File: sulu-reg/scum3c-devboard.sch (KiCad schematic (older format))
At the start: 36 parts, among them J1 Conn_02x11_Odd_Even, J2 Conn_02x10_Odd_Even, J3 Conn_02x05_Odd_Even, J4 73391-0060, U2 S-85S1AB18-I6T1U, U3 S-85S1AB11-I6T1U, U9AB1 ICM-20948

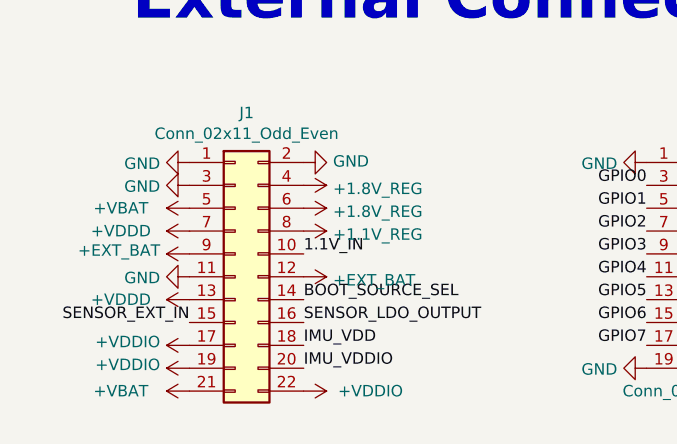
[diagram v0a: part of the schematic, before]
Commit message: Revert "rearranged some architecture"
This reverts commit c12dfdee068bb4749b85b6faf8935c1bd7e1da4a.
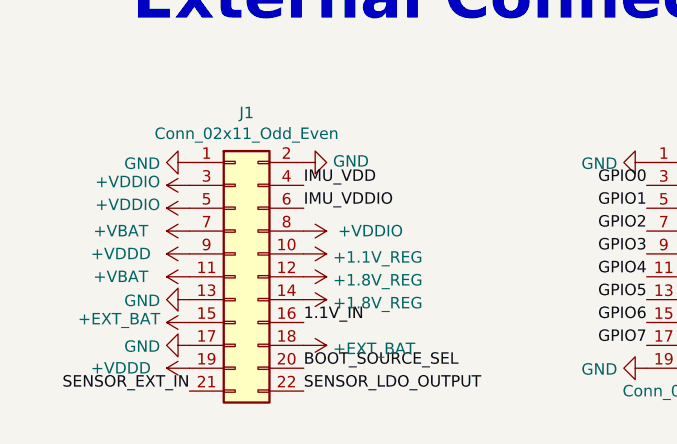
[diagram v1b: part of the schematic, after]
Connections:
- net +1.1V_REG: now also J1.10 (Pin_10); no longer J1.8 (Pin_8)
- net +1.8V_REG: now also J1.12 (Pin_12), J1.14 (Pin_14); no longer J1.4 (Pin_4), J1.6 (Pin_6)
- net +EXT_BAT: now also J1.15 (Pin_15), J1.18 (Pin_18); no longer J1.12 (Pin_12), J1.9 (Pin_9)
- net +VBAT: now also J1.11 (Pin_11), J1.7 (Pin_7); no longer J1.21 (Pin_21), J1.5 (Pin_5)
- net +VDDD: now also J1.19 (Pin_19), J1.9 (Pin_9); no longer J1.13 (Pin_13), J1.7 (Pin_7)
- net +VDDIO: now also J1.3 (Pin_3), J1.5 (Pin_5), J1.8 (Pin_8); no longer J1.17 (Pin_17), J1.19 (Pin_19), J1.22 (Pin_22)
- net 1.1V_IN: now also J1.16 (Pin_16); no longer J1.10 (Pin_10)
- net BOOT_SOURCE_SEL: now also J1.20 (Pin_20); no longer J1.14 (Pin_14)
- net GND: now also J1.13 (Pin_13), J1.17 (Pin_17); no longer J1.11 (Pin_11), J1.3 (Pin_3)
- net IMU_VDD: now also J1.4 (Pin_4); no longer J1.18 (Pin_18)
- net IMU_VDDIO: now also J1.6 (Pin_6); no longer J1.20 (Pin_20)
- net SENSOR_EXT_IN: now also J1.21 (Pin_21); no longer J1.15 (Pin_15)
- net SENSOR_LDO_OUTPUT: now also J1.22 (Pin_22); no longer J1.16 (Pin_16)
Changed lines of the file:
@@
 Text Label 1700 1750 2    50   ~ 0
 IMU_VDDIO
-Text Label 1800 7700 0    50   ~ 0
+Text Label 1800 7000 0    50   ~ 0
 IMU_VDDIO
 Text Label 3800 7300 0    50   ~ 0
@@
 Text Label 3800 7600 0    50   ~ 0
 GPIO15
-Text Label 1800 7600 0    50   ~ 0
+Text Label 1800 6900 0    50   ~ 0
 IMU_VDD
 NoConn ~ 1300 2950
@@
 	0    1    1    0
 $EndComp
-Text Label 1800 7400 0    50   ~ 0
+Text Label 1800 7700 0    50   ~ 0
 BOOT_SOURCE_SEL
 Text Label 5450 7150 0    50   ~ 0
@@
 	0    1    1    0
 $EndComp
-Text Label 1800 7500 0    50   ~ 0
+Text Label 1300 7800 2    50   ~ 0
+SENSOR_EXT_IN
+Text Label 1800 7800 0    50   ~ 0
 SENSOR_LDO_OUTPUT
 Text Label 4950 6950 2    50   ~ 0
@@
 RsTx
 $Comp
+L draft1library:+VDDIO #PWR?
+U 1 1 6076CC41
+P 1300 7000
+AR Path="/5F3B1D81/6076CC41" Ref="#PWR?"  Part="1"
+AR Path="/6076CC41" Ref="#PWR05"  Part="1"
+F 0 "#PWR05" H 1300 6850 50  0001 C CNN
+F 1 "+VDDIO" V 1315 7128 50  0000 L CNN
+F 2 "" H 1300 7000 50  0001 C CNN
+F 3 "" H 1300 7000 50  0001 C CNN
+	1    1300 7000
+	0    -1   -1   0
+$EndComp
+$Comp
+L draft1library:+VDDIO #PWR?
+U 1 1 6076D2AC
+P 1300 6900
+AR Path="/5F3B1D81/6076D2AC" Ref="#PWR?"  Part="1"
+AR Path="/6076D2AC" Ref="#PWR04"  Part="1"
+F 0 "#PWR04" H 1300 6750 50  0001 C CNN
+F 1 "+VDDIO" V 1315 7028 50  0000 L CNN
+F 2 "" H 1300 6900 50  0001 C CNN
+F 3 "" H 1300 6900 50  0001 C CNN
+	1    1300 6900
+	0    -1   -1   0
+$EndComp
+$Comp
 L draft1library:+VBAT #PWR?
 U 1 1 6076D7B9
-P 1300 7800
+P 1300 7100
 AR Path="/5F3B1D81/6076D7B9" Ref="#PWR?"  Part="1"
 AR Path="/5F41418C/6076D7B9" Ref="#PWR?"  Part="1"
 AR Path="/5F414989/6076D7B9" Ref="#PWR?"  Part="1"
 AR Path="/6076D7B9" Ref="#PWR06"  Part="1"
-F 0 "#PWR06" H 1300 7650 50  0001 C CNN
-F 1 "+VBAT" V 1300 8100 50  0000 C CNN
-F 2 "" H 1300 7800 50  0001 C CNN
-F 3 "" H 1300 7800 50  0001 C CNN
-	1    1300 7800
+F 0 "#PWR06" H 1300 6950 50  0001 C CNN
+F 1 "+VBAT" V 1300 7400 50  0000 C CNN
+F 2 "" H 1300 7100 50  0001 C CNN
+F 3 "" H 1300 7100 50  0001 C CNN
+	1    1300 7100
 	0    -1   -1   0
 $EndComp
@@
 L draft1library:+VBAT #PWR?
 U 1 1 6127ADAC
-P 1300 7000
+P 1300 7300
 AR Path="/5F3B1D81/6127ADAC" Ref="#PWR?"  Part="1"
 AR Path="/5F41418C/6127ADAC" Ref="#PWR?"  Part="1"
 AR Path="/5F414989/6127ADAC" Ref="#PWR?"  Part="1"
 AR Path="/6127ADAC" Ref="#PWR0107"  Part="1"
-F 0 "#PWR0107" H 1300 6850 50  0001 C CNN
-F 1 "+VBAT" V 1300 7300 50  0000 C CNN
-F 2 "" H 1300 7000 50  0001 C CNN
-F 3 "" H 1300 7000 50  0001 C CNN
-	1    1300 7000
+F 0 "#PWR0107" H 1300 7150 50  0001 C CNN
+F 1 "+VBAT" V 1300 7600 50  0000 C CNN
+F 2 "" H 1300 7300 50  0001 C CNN
+F 3 "" H 1300 7300 50  0001 C CNN
+	1    1300 7300
 	0    -1   -1   0
 $EndComp
@@
 L power:GND #PWR0108
 U 1 1 6127B18B
-P 1300 6900
-F 0 "#PWR0108" H 1300 6650 50  0001 C CNN
-F 1 "GND" V 1305 6772 50  0000 R CNN
-F 2 "" H 1300 6900 50  0001 C CNN
-F 3 "" H 1300 6900 50  0001 C CNN
-	1    1300 6900
+P 1300 7400
+F 0 "#PWR0108" H 1300 7150 50  0001 C CNN
+F 1 "GND" V 1305 7272 50  0000 R CNN
+F 2 "" H 1300 7400 50  0001 C CNN
+F 3 "" H 1300 7400 50  0001 C CNN
+	1    1300 7400
+	0    1    1    0
+$EndComp
+$Comp
+L power:GND #PWR0109
+U 1 1 6127B4FF
+P 1300 7600
+F 0 "#PWR0109" H 1300 7350 50  0001 C CNN
+F 1 "GND" V 1305 7472 50  0000 R CNN
+F 2 "" H 1300 7600 50  0001 C CNN
+F 3 "" H 1300 7600 50  0001 C CNN
+	1    1300 7600
 	0    1    1    0
 $EndComp
@@
 L draft1library:+1.1V_REG #PWR0110
 U 1 1 61280E78
-P 1800 7100
-F 0 "#PWR0110" H 1800 6950 50  0001 C CNN
-F 1 "+1.1V_REG" V 1815 7228 50  0000 L CNN
-F 2 "" H 1800 7100 50  0001 C CNN
-F 3 "" H 1800 7100 50  0001 C CNN
-	1    1800 7100
+P 1800 7200
+F 0 "#PWR0110" H 1800 7050 50  0001 C CNN
+F 1 "+1.1V_REG" V 1815 7328 50  0000 L CNN
+F 2 "" H 1800 7200 50  0001 C CNN
+F 3 "" H 1800 7200 50  0001 C CNN
+	1    1800 7200
 	0    1    1    0
 $EndComp
@@
 L draft1library:+1.8V_REG #PWR0111
 U 1 1 61281B91
-P 1800 6900
-F 0 "#PWR0111" H 1800 6750 50  0001 C CNN
-F 1 "+1.8V_REG" V 1815 7028 50  0000 L CNN
-F 2 "" H 1800 6900 50  0001 C CNN
-F 3 "" H 1800 6900 50  0001 C CNN
-	1    1800 6900
-	0    1    1    0
-$EndComp
-$Comp
-L draft1library:+1.8V_REG #PWR0112
-U 1 1 612829BE
-P 1800 7000
-F 0 "#PWR0112" H 1800 6850 50  0001 C CNN
-F 1 "+1.8V_REG" V 1815 7128 50  0000 L CNN
-F 2 "" H 1800 7000 50  0001 C CNN
-F 3 "" H 1800 7000 50  0001 C CNN
-	1    1800 7000
-	0    1    1    0
-$EndComp
-$Comp
-L draft1library:+EXT_BAT #PWR0113
-U 1 1 612835E6
 P 1800 7300
-F 0 "#PWR0113" H 1800 7150 50  0001 C CNN
-F 1 "+EXT_BAT" V 1815 7428 50  0000 L CNN
+F 0 "#PWR0111" H 1800 7150 50  0001 C CNN
+F 1 "+1.8V_REG" V 1815 7428 50  0000 L CNN
 F 2 "" H 1800 7300 50  0001 C CNN
 F 3 "" H 1800 7300 50  0001 C CNN
 	1    1800 7300
+	0    1    1    0
+$EndComp
+$Comp
+L draft1library:+1.8V_REG #PWR0112
+U 1 1 612829BE
+P 1800 7400
+F 0 "#PWR0112" H 1800 7250 50  0001 C CNN
+F 1 "+1.8V_REG" V 1815 7528 50  0000 L CNN
+F 2 "" H 1800 7400 50  0001 C CNN
+F 3 "" H 1800 7400 50  0001 C CNN
+	1    1800 7400
+	0    1    1    0
+$EndComp
+$Comp
+L draft1library:+EXT_BAT #PWR0113
+U 1 1 612835E6
+P 1800 7600
+F 0 "#PWR0113" H 1800 7450 50  0001 C CNN
+F 1 "+EXT_BAT" V 1815 7728 50  0000 L CNN
+F 2 "" H 1800 7600 50  0001 C CNN
+F 3 "" H 1800 7600 50  0001 C CNN
+	1    1800 7600
 	0    1    1    0
 $EndComp
@@
 L draft1library:+VDDD #PWR0125
 U 1 1 612C7D86
-P 1300 7100
-F 0 "#PWR0125" H 1300 6950 50  0001 C CNN
-F 1 "+VDDD" V 1300 7400 50  0000 C CNN
-F 2 "" H 1300 7100 50  0001 C CNN
-F 3 "" H 1300 7100 50  0001 C CNN
-	1    1300 7100
+P 1300 7200
+F 0 "#PWR0125" H 1300 7050 50  0001 C CNN
+F 1 "+VDDD" V 1300 7500 50  0000 C CNN
+F 2 "" H 1300 7200 50  0001 C CNN
+F 3 "" H 1300 7200 50  0001 C CNN
+	1    1300 7200
+	0    -1   -1   0
+$EndComp
+$Comp
+L draft1library:+VDDIO #PWR?
+U 1 1 6076E794
+P 1800 7100
+AR Path="/5F3B1D81/6076E794" Ref="#PWR?"  Part="1"
+AR Path="/6076E794" Ref="#PWR08"  Part="1"
+F 0 "#PWR08" H 1800 6950 50  0001 C CNN
+F 1 "+VDDIO" V 1800 7250 50  0000 L CNN
+F 2 "" H 1800 7100 50  0001 C CNN
+F 3 "" H 1800 7100 50  0001 C CNN
+	1    1800 7100
+	0    1    1    0
+$EndComp
+$Comp
+L draft1library:+VDDD #PWR07
+U 1 1 60769F1D
+P 1300 7700
+F 0 "#PWR07" H 1300 7550 50  0001 C CNN
+F 1 "+VDDD" V 1300 8000 50  0000 C CNN
+F 2 "" H 1300 7700 50  0001 C CNN
+F 3 "" H 1300 7700 50  0001 C CNN
+	1    1300 7700
 	0    -1   -1   0
 $EndComp
@@
 	1    0    0    -1
 $EndComp
-Text Label 1800 7200 0    50   ~ 0
+Text Label 1800 7500 0    50   ~ 0
 1.1V_IN
+$Comp
+L draft1library:+EXT_BAT #PWR0123
+U 1 1 6136676E
+P 1300 7500
+F 0 "#PWR0123" H 1300 7350 50  0001 C CNN
+F 1 "+EXT_BAT" V 1315 7628 50  0000 L CNN
+F 2 "" H 1300 7500 50  0001 C CNN
+F 3 "" H 1300 7500 50  0001 C CNN
+	1    1300 7500
+	0    -1   -1   0
+$EndComp
 Text Label 1200 5300 2    50   ~ 0
 1.1V_IN
@@
 $Comp
 L 73391-0060:73391-0060 J4
-U 1 1 61345EE5
+U 1 1 613314E8
 P 4650 2250
 F 0 "J4" H 4612 2564 50  0000 C CNN
@@
 	1    0    0    -1
 $EndComp
-$Comp
-L draft1library:+VDDIO #PWR?
-U 1 1 6076E794
-P 1800 7800
-AR Path="/5F3B1D81/6076E794" Ref="#PWR?"  Part="1"
-AR Path="/6076E794" Ref="#PWR08"  Part="1"
-F 0 "#PWR08" H 1800 7650 50  0001 C CNN
-F 1 "+VDDIO" V 1800 7950 50  0000 L CNN
-F 2 "" H 1800 7800 50  0001 C CNN
-F 3 "" H 1800 7800 50  0001 C CNN
-	1    1800 7800
-	0    1    1    0
-$EndComp
-$Comp
-L draft1library:+EXT_BAT #PWR0123
-U 1 1 6136676E
-P 1300 7200
-F 0 "#PWR0123" H 1300 7050 50  0001 C CNN
-F 1 "+EXT_BAT" V 1315 7328 50  0000 L CNN
-F 2 "" H 1300 7200 50  0001 C CNN
-F 3 "" H 1300 7200 50  0001 C CNN
-	1    1300 7200
-	0    -1   -1   0
-$EndComp
-$Comp
-L draft1library:+VDDD #PWR07
-U 1 1 60769F1D
-P 1300 7400
-F 0 "#PWR07" H 1300 7250 50  0001 C CNN
-F 1 "+VDDD" V 1300 7700 50  0000 C CNN
-F 2 "" H 1300 7400 50  0001 C CNN
-F 3 "" H 1300 7400 50  0001 C CNN
-	1    1300 7400
-	0    -1   -1   0
-$EndComp
-$Comp
-L power:GND #PWR0109
-U 1 1 6127B4FF
-P 1300 7300
-F 0 "#PWR0109" H 1300 7050 50  0001 C CNN
-F 1 "GND" V 1305 7172 50  0000 R CNN
-F 2 "" H 1300 7300 50  0001 C CNN
-F 3 "" H 1300 7300 50  0001 C CNN
-	1    1300 7300
-	0    1    1    0
-$EndComp
-$Comp
-L draft1library:+VDDIO #PWR?
-U 1 1 6076D2AC
-P 1300 7600
-AR Path="/5F3B1D81/6076D2AC" Ref="#PWR?"  Part="1"
-AR Path="/6076D2AC" Ref="#PWR04"  Part="1"
-F 0 "#PWR04" H 1300 7450 50  0001 C CNN
-F 1 "+VDDIO" V 1315 7728 50  0000 L CNN
-F 2 "" H 1300 7600 50  0001 C CNN
-F 3 "" H 1300 7600 50  0001 C CNN
-	1    1300 7600
-	0    -1   -1   0
-$EndComp
-$Comp
-L draft1library:+VDDIO #PWR?
-U 1 1 6076CC41
-P 1300 7700
-AR Path="/5F3B1D81/6076CC41" Ref="#PWR?"  Part="1"
-AR Path="/6076CC41" Ref="#PWR05"  Part="1"
-F 0 "#PWR05" H 1300 7550 50  0001 C CNN
-F 1 "+VDDIO" V 1315 7828 50  0000 L CNN
-F 2 "" H 1300 7700 50  0001 C CNN
-F 3 "" H 1300 7700 50  0001 C CNN
-	1    1300 7700
-	0    -1   -1   0
-$EndComp
-Text Label 1300 7500 2    50   ~ 0
-SENSOR_EXT_IN
 $EndSCHEMATC

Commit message: rearranged some architecture
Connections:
- net +1.1V_REG: now also J1.8 (Pin_8); no longer J1.10 (Pin_10)
- net +1.8V_REG: now also J1.4 (Pin_4), J1.6 (Pin_6); no longer J1.12 (Pin_12), J1.14 (Pin_14)
- net +EXT_BAT: now also J1.12 (Pin_12), J1.9 (Pin_9); no longer J1.15 (Pin_15), J1.18 (Pin_18)
- net +VBAT: now also J1.21 (Pin_21), J1.5 (Pin_5); no longer J1.11 (Pin_11), J1.7 (Pin_7)
- net +VDDD: now also J1.13 (Pin_13), J1.7 (Pin_7); no longer J1.19 (Pin_19), J1.9 (Pin_9)
- net +VDDIO: now also J1.17 (Pin_17), J1.19 (Pin_19), J1.22 (Pin_22); no longer J1.3 (Pin_3), J1.5 (Pin_5), J1.8 (Pin_8)
- net 1.1V_IN: now also J1.10 (Pin_10); no longer J1.16 (Pin_16)
- net BOOT_SOURCE_SEL: now also J1.14 (Pin_14); no longer J1.20 (Pin_20)
- net GND: now also J1.11 (Pin_11), J1.3 (Pin_3); no longer J1.13 (Pin_13), J1.17 (Pin_17)
- net IMU_VDD: now also J1.18 (Pin_18); no longer J1.4 (Pin_4)
- net IMU_VDDIO: now also J1.20 (Pin_20); no longer J1.6 (Pin_6)
- net SENSOR_EXT_IN: now also J1.15 (Pin_15); no longer J1.21 (Pin_21)
- net SENSOR_LDO_OUTPUT: now also J1.16 (Pin_16); no longer J1.22 (Pin_22)
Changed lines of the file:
@@
 Text Label 1700 1750 2    50   ~ 0
 IMU_VDDIO
-Text Label 1800 7000 0    50   ~ 0
+Text Label 1800 7700 0    50   ~ 0
 IMU_VDDIO
 Text Label 3800 7300 0    50   ~ 0
@@
 Text Label 3800 7600 0    50   ~ 0
 GPIO15
-Text Label 1800 6900 0    50   ~ 0
+Text Label 1800 7600 0    50   ~ 0
 IMU_VDD
 NoConn ~ 1300 2950
@@
 	0    1    1    0
 $EndComp
-Text Label 1800 7700 0    50   ~ 0
+Text Label 1800 7400 0    50   ~ 0
 BOOT_SOURCE_SEL
 Text Label 5450 7150 0    50   ~ 0
@@
 	0    1    1    0
 $EndComp
-Text Label 1300 7800 2    50   ~ 0
-SENSOR_EXT_IN
-Text Label 1800 7800 0    50   ~ 0
+Text Label 1800 7500 0    50   ~ 0
 SENSOR_LDO_OUTPUT
 Text Label 4950 6950 2    50   ~ 0
@@
 RsTx
 $Comp
-L draft1library:+VDDIO #PWR?
-U 1 1 6076CC41
-P 1300 7000
-AR Path="/5F3B1D81/6076CC41" Ref="#PWR?"  Part="1"
-AR Path="/6076CC41" Ref="#PWR05"  Part="1"
-F 0 "#PWR05" H 1300 6850 50  0001 C CNN
-F 1 "+VDDIO" V 1315 7128 50  0000 L CNN
-F 2 "" H 1300 7000 50  0001 C CNN
-F 3 "" H 1300 7000 50  0001 C CNN
-	1    1300 7000
-	0    -1   -1   0
-$EndComp
-$Comp
-L draft1library:+VDDIO #PWR?
-U 1 1 6076D2AC
-P 1300 6900
-AR Path="/5F3B1D81/6076D2AC" Ref="#PWR?"  Part="1"
-AR Path="/6076D2AC" Ref="#PWR04"  Part="1"
-F 0 "#PWR04" H 1300 6750 50  0001 C CNN
-F 1 "+VDDIO" V 1315 7028 50  0000 L CNN
-F 2 "" H 1300 6900 50  0001 C CNN
-F 3 "" H 1300 6900 50  0001 C CNN
-	1    1300 6900
-	0    -1   -1   0
-$EndComp
-$Comp
 L draft1library:+VBAT #PWR?
 U 1 1 6076D7B9
-P 1300 7100
+P 1300 7800
 AR Path="/5F3B1D81/6076D7B9" Ref="#PWR?"  Part="1"
 AR Path="/5F41418C/6076D7B9" Ref="#PWR?"  Part="1"
 AR Path="/5F414989/6076D7B9" Ref="#PWR?"  Part="1"
 AR Path="/6076D7B9" Ref="#PWR06"  Part="1"
-F 0 "#PWR06" H 1300 6950 50  0001 C CNN
-F 1 "+VBAT" V 1300 7400 50  0000 C CNN
-F 2 "" H 1300 7100 50  0001 C CNN
-F 3 "" H 1300 7100 50  0001 C CNN
-	1    1300 7100
+F 0 "#PWR06" H 1300 7650 50  0001 C CNN
+F 1 "+VBAT" V 1300 8100 50  0000 C CNN
+F 2 "" H 1300 7800 50  0001 C CNN
+F 3 "" H 1300 7800 50  0001 C CNN
+	1    1300 7800
 	0    -1   -1   0
 $EndComp
@@
 L draft1library:+VBAT #PWR?
 U 1 1 6127ADAC
-P 1300 7300
+P 1300 7000
 AR Path="/5F3B1D81/6127ADAC" Ref="#PWR?"  Part="1"
 AR Path="/5F41418C/6127ADAC" Ref="#PWR?"  Part="1"
 AR Path="/5F414989/6127ADAC" Ref="#PWR?"  Part="1"
 AR Path="/6127ADAC" Ref="#PWR0107"  Part="1"
-F 0 "#PWR0107" H 1300 7150 50  0001 C CNN
-F 1 "+VBAT" V 1300 7600 50  0000 C CNN
-F 2 "" H 1300 7300 50  0001 C CNN
-F 3 "" H 1300 7300 50  0001 C CNN
-	1    1300 7300
+F 0 "#PWR0107" H 1300 6850 50  0001 C CNN
+F 1 "+VBAT" V 1300 7300 50  0000 C CNN
+F 2 "" H 1300 7000 50  0001 C CNN
+F 3 "" H 1300 7000 50  0001 C CNN
+	1    1300 7000
 	0    -1   -1   0
 $EndComp
@@
 L power:GND #PWR0108
 U 1 1 6127B18B
-P 1300 7400
-F 0 "#PWR0108" H 1300 7150 50  0001 C CNN
-F 1 "GND" V 1305 7272 50  0000 R CNN
-F 2 "" H 1300 7400 50  0001 C CNN
-F 3 "" H 1300 7400 50  0001 C CNN
-	1    1300 7400
-	0    1    1    0
-$EndComp
-$Comp
-L power:GND #PWR0109
-U 1 1 6127B4FF
-P 1300 7600
-F 0 "#PWR0109" H 1300 7350 50  0001 C CNN
-F 1 "GND" V 1305 7472 50  0000 R CNN
-F 2 "" H 1300 7600 50  0001 C CNN
-F 3 "" H 1300 7600 50  0001 C CNN
-	1    1300 7600
+P 1300 6900
+F 0 "#PWR0108" H 1300 6650 50  0001 C CNN
+F 1 "GND" V 1305 6772 50  0000 R CNN
+F 2 "" H 1300 6900 50  0001 C CNN
+F 3 "" H 1300 6900 50  0001 C CNN
+	1    1300 6900
 	0    1    1    0
 $EndComp
@@
 L draft1library:+1.1V_REG #PWR0110
 U 1 1 61280E78
-P 1800 7200
-F 0 "#PWR0110" H 1800 7050 50  0001 C CNN
-F 1 "+1.1V_REG" V 1815 7328 50  0000 L CNN
-F 2 "" H 1800 7200 50  0001 C CNN
-F 3 "" H 1800 7200 50  0001 C CNN
-	1    1800 7200
+P 1800 7100
+F 0 "#PWR0110" H 1800 6950 50  0001 C CNN
+F 1 "+1.1V_REG" V 1815 7228 50  0000 L CNN
+F 2 "" H 1800 7100 50  0001 C CNN
+F 3 "" H 1800 7100 50  0001 C CNN
+	1    1800 7100
 	0    1    1    0
 $EndComp
@@
 L draft1library:+1.8V_REG #PWR0111
 U 1 1 61281B91
+P 1800 6900
+F 0 "#PWR0111" H 1800 6750 50  0001 C CNN
+F 1 "+1.8V_REG" V 1815 7028 50  0000 L CNN
+F 2 "" H 1800 6900 50  0001 C CNN
+F 3 "" H 1800 6900 50  0001 C CNN
+	1    1800 6900
+	0    1    1    0
+$EndComp
+$Comp
+L draft1library:+1.8V_REG #PWR0112
+U 1 1 612829BE
+P 1800 7000
+F 0 "#PWR0112" H 1800 6850 50  0001 C CNN
+F 1 "+1.8V_REG" V 1815 7128 50  0000 L CNN
+F 2 "" H 1800 7000 50  0001 C CNN
+F 3 "" H 1800 7000 50  0001 C CNN
+	1    1800 7000
+	0    1    1    0
+$EndComp
+$Comp
+L draft1library:+EXT_BAT #PWR0113
+U 1 1 612835E6
 P 1800 7300
-F 0 "#PWR0111" H 1800 7150 50  0001 C CNN
-F 1 "+1.8V_REG" V 1815 7428 50  0000 L CNN
+F 0 "#PWR0113" H 1800 7150 50  0001 C CNN
+F 1 "+EXT_BAT" V 1815 7428 50  0000 L CNN
 F 2 "" H 1800 7300 50  0001 C CNN
 F 3 "" H 1800 7300 50  0001 C CNN
 	1    1800 7300
-	0    1    1    0
-$EndComp
-$Comp
-L draft1library:+1.8V_REG #PWR0112
-U 1 1 612829BE
-P 1800 7400
-F 0 "#PWR0112" H 1800 7250 50  0001 C CNN
-F 1 "+1.8V_REG" V 1815 7528 50  0000 L CNN
-F 2 "" H 1800 7400 50  0001 C CNN
-F 3 "" H 1800 7400 50  0001 C CNN
-	1    1800 7400
-	0    1    1    0
-$EndComp
-$Comp
-L draft1library:+EXT_BAT #PWR0113
-U 1 1 612835E6
-P 1800 7600
-F 0 "#PWR0113" H 1800 7450 50  0001 C CNN
-F 1 "+EXT_BAT" V 1815 7728 50  0000 L CNN
-F 2 "" H 1800 7600 50  0001 C CNN
-F 3 "" H 1800 7600 50  0001 C CNN
-	1    1800 7600
 	0    1    1    0
 $EndComp
@@
 L draft1library:+VDDD #PWR0125
 U 1 1 612C7D86
-P 1300 7200
-F 0 "#PWR0125" H 1300 7050 50  0001 C CNN
-F 1 "+VDDD" V 1300 7500 50  0000 C CNN
-F 2 "" H 1300 7200 50  0001 C CNN
-F 3 "" H 1300 7200 50  0001 C CNN
-	1    1300 7200
-	0    -1   -1   0
-$EndComp
-$Comp
-L draft1library:+VDDIO #PWR?
-U 1 1 6076E794
-P 1800 7100
-AR Path="/5F3B1D81/6076E794" Ref="#PWR?"  Part="1"
-AR Path="/6076E794" Ref="#PWR08"  Part="1"
-F 0 "#PWR08" H 1800 6950 50  0001 C CNN
-F 1 "+VDDIO" V 1800 7250 50  0000 L CNN
-F 2 "" H 1800 7100 50  0001 C CNN
-F 3 "" H 1800 7100 50  0001 C CNN
-	1    1800 7100
-	0    1    1    0
-$EndComp
-$Comp
-L draft1library:+VDDD #PWR07
-U 1 1 60769F1D
-P 1300 7700
-F 0 "#PWR07" H 1300 7550 50  0001 C CNN
-F 1 "+VDDD" V 1300 8000 50  0000 C CNN
-F 2 "" H 1300 7700 50  0001 C CNN
-F 3 "" H 1300 7700 50  0001 C CNN
-	1    1300 7700
+P 1300 7100
+F 0 "#PWR0125" H 1300 6950 50  0001 C CNN
+F 1 "+VDDD" V 1300 7400 50  0000 C CNN
+F 2 "" H 1300 7100 50  0001 C CNN
+F 3 "" H 1300 7100 50  0001 C CNN
+	1    1300 7100
 	0    -1   -1   0
 $EndComp
@@
 	1    0    0    -1
 $EndComp
-Text Label 1800 7500 0    50   ~ 0
+Text Label 1800 7200 0    50   ~ 0
 1.1V_IN
-$Comp
-L draft1library:+EXT_BAT #PWR0123
-U 1 1 6136676E
-P 1300 7500
-F 0 "#PWR0123" H 1300 7350 50  0001 C CNN
-F 1 "+EXT_BAT" V 1315 7628 50  0000 L CNN
-F 2 "" H 1300 7500 50  0001 C CNN
-F 3 "" H 1300 7500 50  0001 C CNN
-	1    1300 7500
-	0    -1   -1   0
-$EndComp
 Text Label 1200 5300 2    50   ~ 0
 1.1V_IN
@@
 $Comp
 L 73391-0060:73391-0060 J4
-U 1 1 613314E8
+U 1 1 61345EE5
 P 4650 2250
 F 0 "J4" H 4612 2564 50  0000 C CNN
@@
 	1    0    0    -1
 $EndComp
+$Comp
+L draft1library:+VDDIO #PWR?
+U 1 1 6076E794
+P 1800 7800
+AR Path="/5F3B1D81/6076E794" Ref="#PWR?"  Part="1"
+AR Path="/6076E794" Ref="#PWR08"  Part="1"
+F 0 "#PWR08" H 1800 7650 50  0001 C CNN
+F 1 "+VDDIO" V 1800 7950 50  0000 L CNN
+F 2 "" H 1800 7800 50  0001 C CNN
+F 3 "" H 1800 7800 50  0001 C CNN
+	1    1800 7800
+	0    1    1    0
+$EndComp
+$Comp
+L draft1library:+EXT_BAT #PWR0123
+U 1 1 6136676E
+P 1300 7200
+F 0 "#PWR0123" H 1300 7050 50  0001 C CNN
+F 1 "+EXT_BAT" V 1315 7328 50  0000 L CNN
+F 2 "" H 1300 7200 50  0001 C CNN
+F 3 "" H 1300 7200 50  0001 C CNN
+	1    1300 7200
+	0    -1   -1   0
+$EndComp
+$Comp
+L draft1library:+VDDD #PWR07
+U 1 1 60769F1D
+P 1300 7400
+F 0 "#PWR07" H 1300 7250 50  0001 C CNN
+F 1 "+VDDD" V 1300 7700 50  0000 C CNN
+F 2 "" H 1300 7400 50  0001 C CNN
+F 3 "" H 1300 7400 50  0001 C CNN
+	1    1300 7400
+	0    -1   -1   0
+$EndComp
+$Comp
+L power:GND #PWR0109
+U 1 1 6127B4FF
+P 1300 7300
+F 0 "#PWR0109" H 1300 7050 50  0001 C CNN
+F 1 "GND" V 1305 7172 50  0000 R CNN
+F 2 "" H 1300 7300 50  0001 C CNN
+F 3 "" H 1300 7300 50  0001 C CNN
+	1    1300 7300
+	0    1    1    0
+$EndComp
+$Comp
+L draft1library:+VDDIO #PWR?
+U 1 1 6076D2AC
+P 1300 7600
+AR Path="/5F3B1D81/6076D2AC" Ref="#PWR?"  Part="1"
+AR Path="/6076D2AC" Ref="#PWR04"  Part="1"
+F 0 "#PWR04" H 1300 7450 50  0001 C CNN
+F 1 "+VDDIO" V 1315 7728 50  0000 L CNN
+F 2 "" H 1300 7600 50  0001 C CNN
+F 3 "" H 1300 7600 50  0001 C CNN
+	1    1300 7600
+	0    -1   -1   0
+$EndComp
+$Comp
+L draft1library:+VDDIO #PWR?
+U 1 1 6076CC41
+P 1300 7700
+AR Path="/5F3B1D81/6076CC41" Ref="#PWR?"  Part="1"
+AR Path="/6076CC41" Ref="#PWR05"  Part="1"
+F 0 "#PWR05" H 1300 7550 50  0001 C CNN
+F 1 "+VDDIO" V 1315 7828 50  0000 L CNN
+F 2 "" H 1300 7700 50  0001 C CNN
+F 3 "" H 1300 7700 50  0001 C CNN
+	1    1300 7700
+	0    -1   -1   0
+$EndComp
+Text Label 1300 7500 2    50   ~ 0
+SENSOR_EXT_IN
 $EndSCHEMATC
